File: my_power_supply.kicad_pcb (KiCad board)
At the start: 2 copper layers, 85 x 37.5 mm, 11 parts, among them U2 TPS54560BDDA, U3 HUSB238, U4 TPS54560BDDA

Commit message: V1 progress
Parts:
- added C1: 1u, Capacitor_SMD:C_1206_3216Metric, F.Cu at (113.0, 139.5)
- added J1: USB_C_Receptacle_USB2.0_16P, Connector_USB:USB_C_Receptacle_GCT_USB4135-GF-A_6P_TopMnt_Horizontal, F.Cu at (103.5, 132.2)
- moved R4 87.3 mm to (125.0, 129.6)
- moved R3 87.3 mm to (125.0, 126.3)
- moved R5 87.3 mm to (125.0, 132.9)
- moved R2 87.3 mm to (125.0, 123.0)
- moved R6 87.3 mm to (125.0, 136.2)
- moved R7 87.3 mm to (125.0, 139.4)
- moved R1 69.9 mm to (113.5, 122.0)
- moved R8 69.1 mm to (113.5, 125.0)
- moved U3 34.3 mm to (113.5, 131.5), turned to 180 degrees
- moved U2 29.5 mm to (146.3, 127.2)
- moved U4 27.3 mm to (146.2, 137.2)

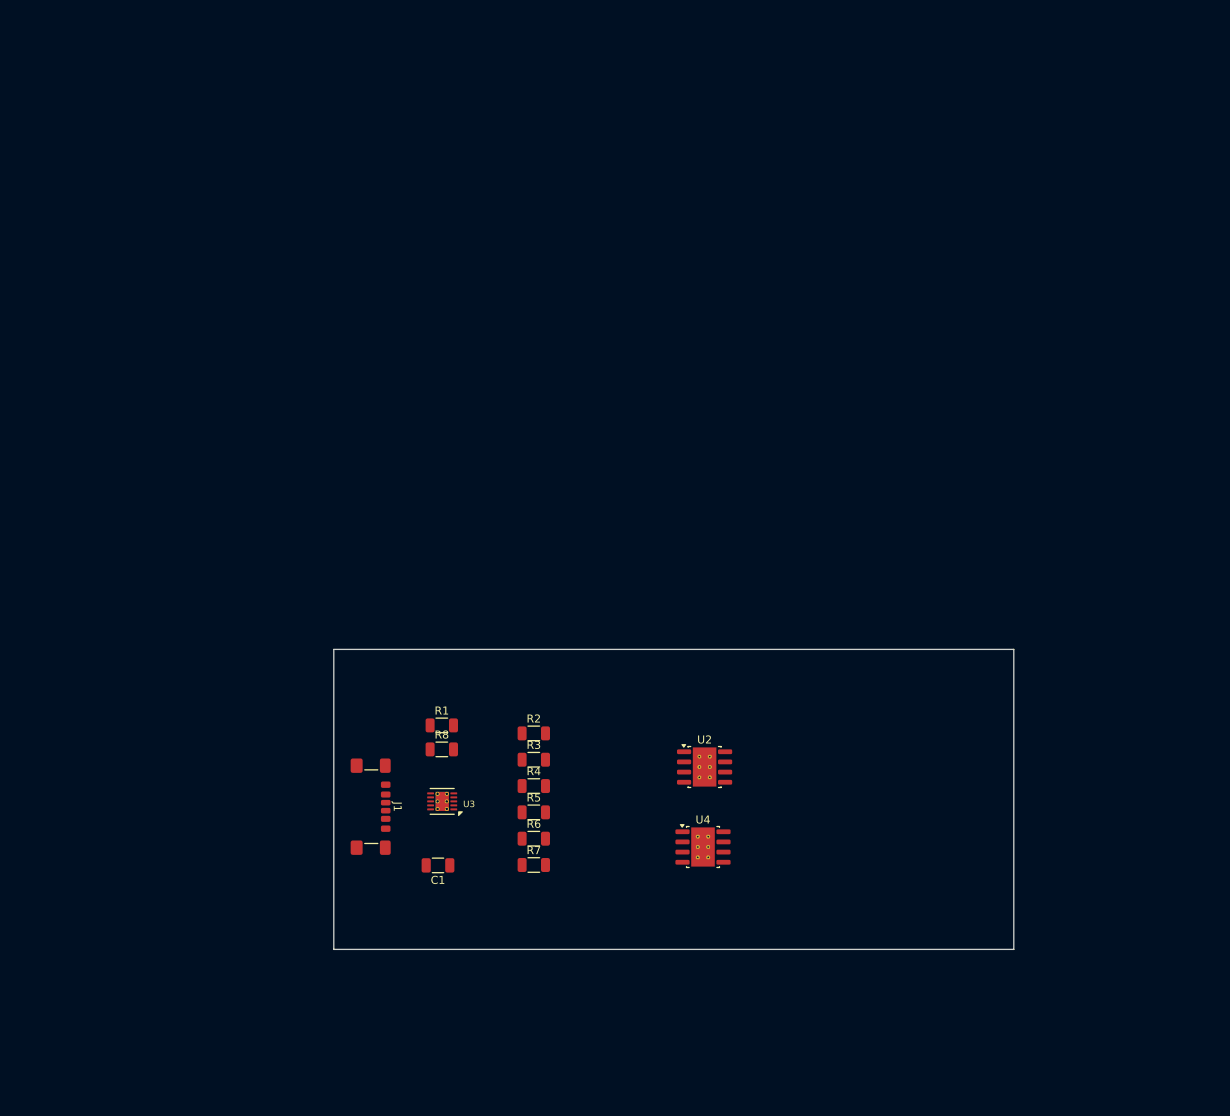
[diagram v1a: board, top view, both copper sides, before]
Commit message: Add footprints for some modules, everything has some kind of footprint to start. Beginning of layout
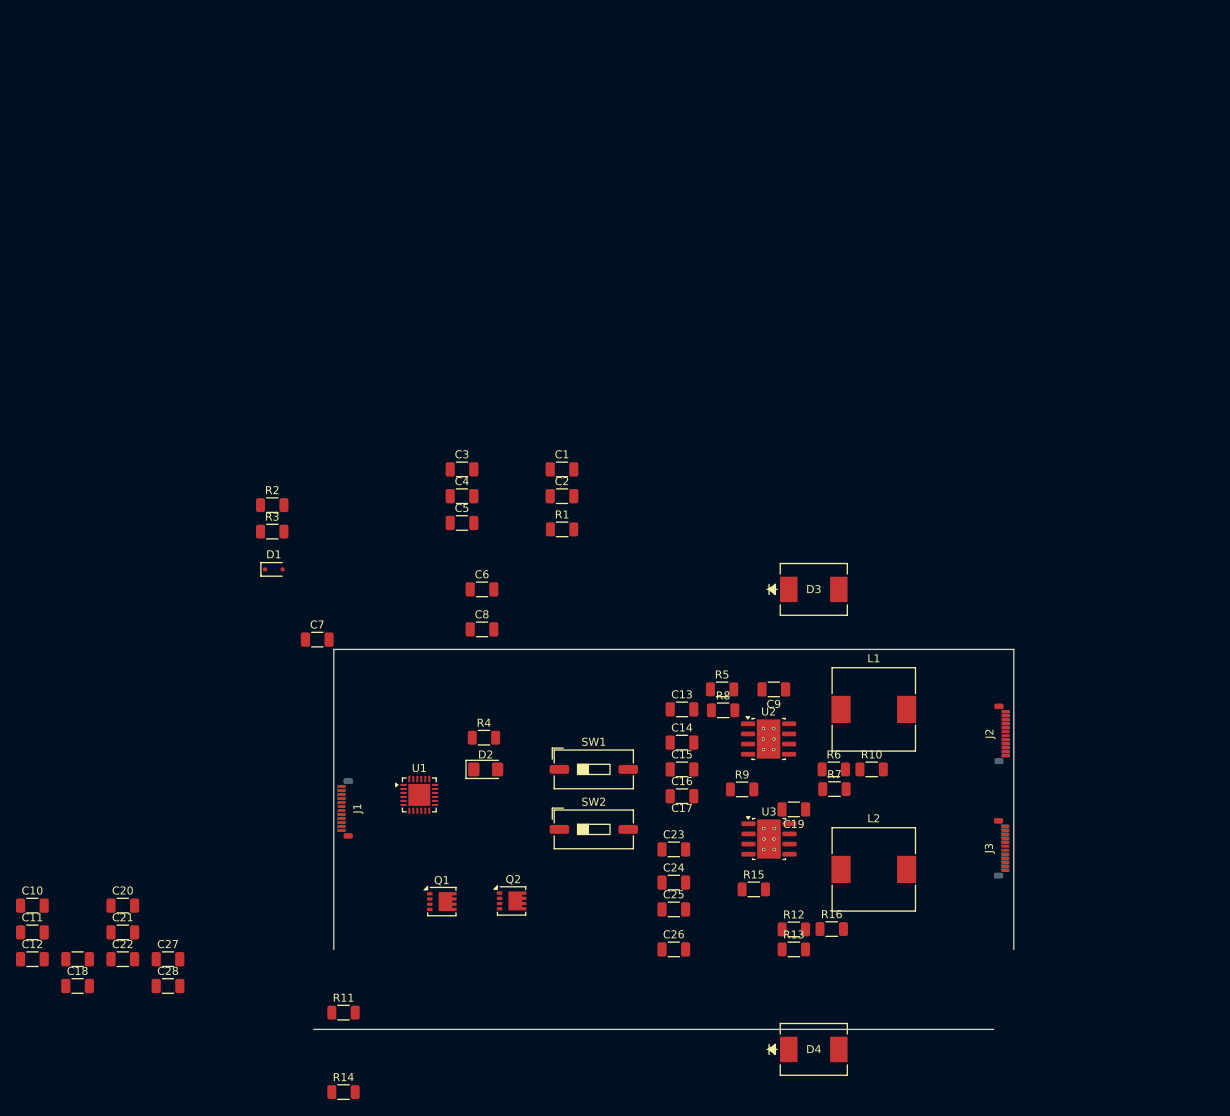
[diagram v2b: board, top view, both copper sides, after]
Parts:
- removed U4: TPS54560BDDA, Package_SO:Texas_R-PDSO-G8_EP2.95x4.9mm_Mask2.4x3.1mm_ThermalVias
- added C10: 47u, Capacitor_SMD:C_1206_3216Metric, F.Cu at (62.3, 144.5)
- added C11: 47u, Capacitor_SMD:C_1206_3216Metric, F.Cu at (62.3, 147.9)
- added C12: 47u, Capacitor_SMD:C_1206_3216Metric, F.Cu at (62.3, 151.2)
- added C13: 2.2u, Capacitor_SMD:C_1206_3216Metric, F.Cu at (143.5, 120.0)
- added C14: 2.2u, Capacitor_SMD:C_1206_3216Metric, F.Cu at (143.5, 124.2)
- added C15: 2.2u, Capacitor_SMD:C_1206_3216Metric, F.Cu at (143.5, 127.5)
- added C16: 2.2u, Capacitor_SMD:C_1206_3216Metric, F.Cu at (143.5, 130.8)
- added C17: 47p, Capacitor_SMD:C_1206_3216Metric, F.Cu at (68.0, 151.2)
- added C18: 4700p, Capacitor_SMD:C_1206_3216Metric, F.Cu at (68.0, 154.6)
- added C19: 0.1u, Capacitor_SMD:C_1206_3216Metric, F.Cu at (157.5, 132.5)
- added C2: 1u, Capacitor_SMD:C_1206_3216Metric, F.Cu at (128.5, 93.3)
- added C20: 47u, Capacitor_SMD:C_1206_3216Metric, F.Cu at (73.6, 144.5)
- added C21: 47u, Capacitor_SMD:C_1206_3216Metric, F.Cu at (73.6, 147.9)
- added C22: 47u, Capacitor_SMD:C_1206_3216Metric, F.Cu at (73.6, 151.2)
- added C23: 2.2u, Capacitor_SMD:C_1206_3216Metric, F.Cu at (142.5, 137.5)
- added C24: 2.2u, Capacitor_SMD:C_1206_3216Metric, F.Cu at (142.5, 141.7)
- added C25: 2.2u, Capacitor_SMD:C_1206_3216Metric, F.Cu at (142.5, 145.0)
- added C26: 2.2u, Capacitor_SMD:C_1206_3216Metric, F.Cu at (142.5, 150.0)
- added C27: 47p, Capacitor_SMD:C_1206_3216Metric, F.Cu at (79.3, 151.2)
- added C28: 4700p, Capacitor_SMD:C_1206_3216Metric, F.Cu at (79.3, 154.6)
- added C3: 1u, Capacitor_SMD:C_1206_3216Metric, F.Cu at (116.0, 90.0)
- added C4: 0.1u, Capacitor_SMD:C_1206_3216Metric, F.Cu at (116.0, 93.3)
- added C5: 0.1u, Capacitor_SMD:C_1206_3216Metric, F.Cu at (116.0, 96.7)
- added C6: 390p, Capacitor_SMD:C_1206_3216Metric, F.Cu at (118.5, 105.0)
- added C7: 1u, Capacitor_SMD:C_1206_3216Metric, F.Cu at (97.9, 111.3)
- added C8: 390p, Capacitor_SMD:C_1206_3216Metric, F.Cu at (118.5, 110.0)
- added C9: 0.1u, Capacitor_SMD:C_1206_3216Metric, F.Cu at (155.0, 117.5)
- added D1: D_Schottky, Diode_SMD:D_SOD-323F, F.Cu at (92.5, 102.5)
- added D2: LED_Small, LED_SMD:LED_1206_3216Metric_Pad1.42x1.75mm_HandSolder, F.Cu at (119.0, 127.5)
- added D3: D_Schottky, imported:SMC_DIO, F.Cu at (160.0, 105.0)
- added D4: D_Schottky, imported:SMC_DIO, F.Cu at (160.0, 162.5)
- added J2: USB_C_Receptacle_PowerOnly_6P, Connector_USB:USB_C_Plug_Molex_105444, F.Cu at (184.0, 123.0)
- added J3: USB_C_Receptacle_PowerOnly_6P, Connector_USB:USB_C_Plug_Molex_105444, F.Cu at (184.0, 137.4)
- added L1: 7.2u, imported:L_Wurth_WE-PDF-1045, F.Cu at (167.5, 120.0)
- added L2: 7.2u, imported:L_Wurth_WE-PDF-1045, F.Cu at (167.5, 140.0)
- added Q1: DMP3013SFV, Package_SON:Diodes_PowerDI3333-8, F.Cu at (113.5, 144.0)
- added Q2: DMP3013SFV, Package_SON:Diodes_PowerDI3333-8, F.Cu at (122.2, 143.9)
- added R10: 10.2k, Resistor_SMD:R_1206_3216Metric, F.Cu at (167.2, 127.5)
- added R11: 442k, Resistor_SMD:R_1206_3216Metric, F.Cu at (101.2, 157.9)
- added R12: 53.6k, Resistor_SMD:R_1206_3216Metric, F.Cu at (157.5, 147.5)
- added R13: 16.9k, Resistor_SMD:R_1206_3216Metric, F.Cu at (157.5, 150.0)
- added R14: 90.9k, Resistor_SMD:R_1206_3216Metric, F.Cu at (101.2, 167.8)
- added R15: 243k, Resistor_SMD:R_1206_3216Metric, F.Cu at (152.5, 142.5)
- added R16: 10.2k, Resistor_SMD:R_1206_3216Metric, F.Cu at (162.2, 147.5)
- added R9: 243k, Resistor_SMD:R_1206_3216Metric, F.Cu at (151.0, 130.0)
- added SW1: SW_SPST, Button_Switch_SMD:SW_DIP_SPSTx01_Slide_9.78x4.72mm_W8.61mm_P2.54mm, F.Cu at (132.5, 127.5)
- added SW2: SW_SPST, Button_Switch_SMD:SW_DIP_SPSTx01_Slide_9.78x4.72mm_W8.61mm_P2.54mm, F.Cu at (132.5, 135.0)
- added U1: CYPD3177-24LQ, Package_DFN_QFN:QFN-24-1EP_4x4mm_P0.5mm_EP2.75x2.75mm, F.Cu at (110.7, 130.7)
- C1: value 1u -> 3.3u
- J1: footprint Connector_USB:USB_C_Receptacle_GCT_USB4135-GF-A_6P_TopMnt_Horizontal -> Connector_USB:USB_C_Plug_Molex_105444
- R1: value 10 -> 10k
- R2: value 5.1k -> 47k
- R3: value 49.9k -> 1k
- R4: value 14k -> 2.4k
- R5: value 6k -> 442k
- R6: value 10k -> 53.6k
- R7: value 14k -> 16.9k
- R8: value 18k -> 90.9k
- U3: value HUSB238 -> TPS54560BDDA; footprint HUSB238:DFN-10-1EP_3x3mm_P0.5mm_EP1.65x2.38mm_ThermalVias -> Package_SO:Texas_R-PDSO-G8_EP2.95x4.9mm_Mask2.4x3.1mm_ThermalVias
- moved C1 51.9 mm to (128.5, 90.0), turned to 0 degrees
- moved R2 43.4 mm to (92.3, 94.5)
- moved R3 43.4 mm to (92.3, 97.8)
- moved U3 41.1 mm to (154.4, 136.2), turned to 0 degrees
- moved R7 38.8 mm to (162.6, 130.0)
- moved R6 38.5 mm to (162.5, 127.5)
- moved R8 35.5 mm to (148.7, 120.1)
- moved R1 28.7 mm to (128.5, 97.5)
- moved R5 28.1 mm to (148.5, 117.5)
- moved U2 8.73 mm to (154.3, 123.7)
- moved R4 8.68 mm to (118.8, 123.5)
- moved J1 2.55 mm to (100.9, 132.4), turned to 90 degrees
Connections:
- C1 pad 1: Net-(U3-VIN) -> VBUSIN
- J1 pad A5: /CC1 -> CC1
- J1 pad A9: Net-(J1-VBUS-PadA4) -> VBUSIN
- J1 pad B5: /CC2 -> CC2
- J1 pad B9: Net-(J1-VBUS-PadA4) -> VBUSIN
- R1 pad 1: Net-(J1-VBUS-PadA4) -> Net-(D1-A)
- R1 pad 2: Net-(U3-VIN) -> VBUSIN
- R2 pad 1: Net-(U3-GATE) -> Net-(D1-A)
- R2 pad 2: Net-(Q1-Pad4) -> Net-(D1-K)
- R3 pad 1: Net-(J1-VBUS-PadA4) -> Net-(U1-VBUS_FET_EN)
- R3 pad 2: Net-(Q1-Pad4) -> Net-(D1-A)
- R4 pad 2: Net-(JP6-A) -> Net-(D2-A)
- R5 pad 1: Net-(JP2-A) -> VCC1
- R5 pad 2: Net-(JP1-A) -> Net-(U2-EN)
- R6 pad 1: Net-(JP3-A) -> VOUT1
- R6 pad 2: Net-(JP1-A) -> FB1
- R7 pad 1: Net-(JP4-A) -> Net-(U2-COMP)
- R7 pad 2: Net-(JP1-A) -> Net-(C18-Pad2)
- R8 pad 1: Net-(JP5-A) -> Net-(U2-EN)
- R8 pad 2: Net-(JP1-A) -> GND
- U3 pad 1: Net-(U3-VIN) -> Net-(U3-BOOT)
- U3 pad 2: /D+ -> VCC2
- U3 pad 3: /D- -> Net-(U3-EN)
- U3 pad 4: /CC1 -> Net-(U3-RT/CLK)
- U3 pad 5: /CC2 -> FB2
- U3 pad 6: unconnected-(U3-SDA-Pad6) -> Net-(U3-COMP)
- U3 pad 7: unconnected-(U3-SCL-Pad7) -> GND
- U3 pad 8: Net-(JP1-A) -> Net-(D4-K)
- U3 pad 9: Net-(JP6-A) -> GND
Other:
- board size 85 x 37.5 mm -> 87.5 x 47.5 mm

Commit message: More PCB layout
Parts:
- moved C12 116.6 mm to (174.2, 118.2), turned to 90 degrees
- moved C11 113.4 mm to (171.8, 118.3), turned to 90 degrees
- moved C10 110.3 mm to (169.4, 118.2), turned to 90 degrees
- moved C17 105.3 mm to (169.1, 121.7), turned to 180 degrees
- moved C18 104.9 mm to (170.0, 130.0)
- moved C22 101.4 mm to (175.0, 152.5), turned to 90 degrees
- moved C21 99.0 mm to (172.5, 152.5), turned to 90 degrees
- moved C20 96.7 mm to (170.0, 152.5), turned to 90 degrees
- moved C27 90.6 mm to (169.7, 156.5), turned to 180 degrees
- moved C28 90.3 mm to (169.0, 165.0), turned to 180 degrees
- moved C1 62.9 mm to (92.4, 141.5), turned to 90 degrees
- moved C3 60.1 mm to (85.0, 141.5), turned to -90 degrees
- moved C2 58.8 mm to (94.8, 141.5), turned to 90 degrees
- moved C4 58.7 mm to (82.5, 141.5), turned to -90 degrees
- moved C5 57.5 mm to (80.0, 141.5), turned to -90 degrees
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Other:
- board outline removed

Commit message: Even more PCB layout
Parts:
- added R17: DNP, Resistor_SMD:R_1206_3216Metric, F.Cu at (93.0, 122.0)
- J1: footprint Connector_USB:USB_C_Plug_Molex_105444 -> Connector_USB:USB_C_Plug_JAE_DX07P024AJ1
- moved Q1 19.6 mm to (81.5, 139.3), turned to 180 degrees
- moved R3 17.0 mm to (90.0, 134.0)
- moved D1 16.8 mm to (85.9, 143.5)
- moved R2 13.2 mm to (94.5, 133.0)
- moved Q2 9.07 mm to (96.0, 138.4)
- moved C1 6.00 mm to (90.0, 147.0)
- moved R1 6.00 mm to (95.1, 147.0)
- moved C2 6.00 mm to (92.4, 147.0)
- moved C3 5.70 mm to (90.5, 140.0)
- moved C4 5.70 mm to (88.0, 140.0)
- moved C5 5.70 mm to (85.5, 140.0)
- moved C7 5.00 mm to (89.5, 136.5), turned to 180 degrees
- moved C8 2.50 mm to (81.0, 128.0)
- moved J1 1.98 mm to (75.5, 133.5), turned to -90 degrees
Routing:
- net Net-(D1-A): track 0.00 -> 17.1 mm
- net Net-(D1-K): track 0.00 -> 14.8 mm
- net CC1: track 0.00 -> 8.46 mm
- net 3V3: track 0.00 -> 7.89 mm
- net GND: track 0.00 -> 7.06 mm
- net Net-(U1-VCCD): track 0.00 -> 2.62 mm
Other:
- board outline added: 5 x 8.2 mm

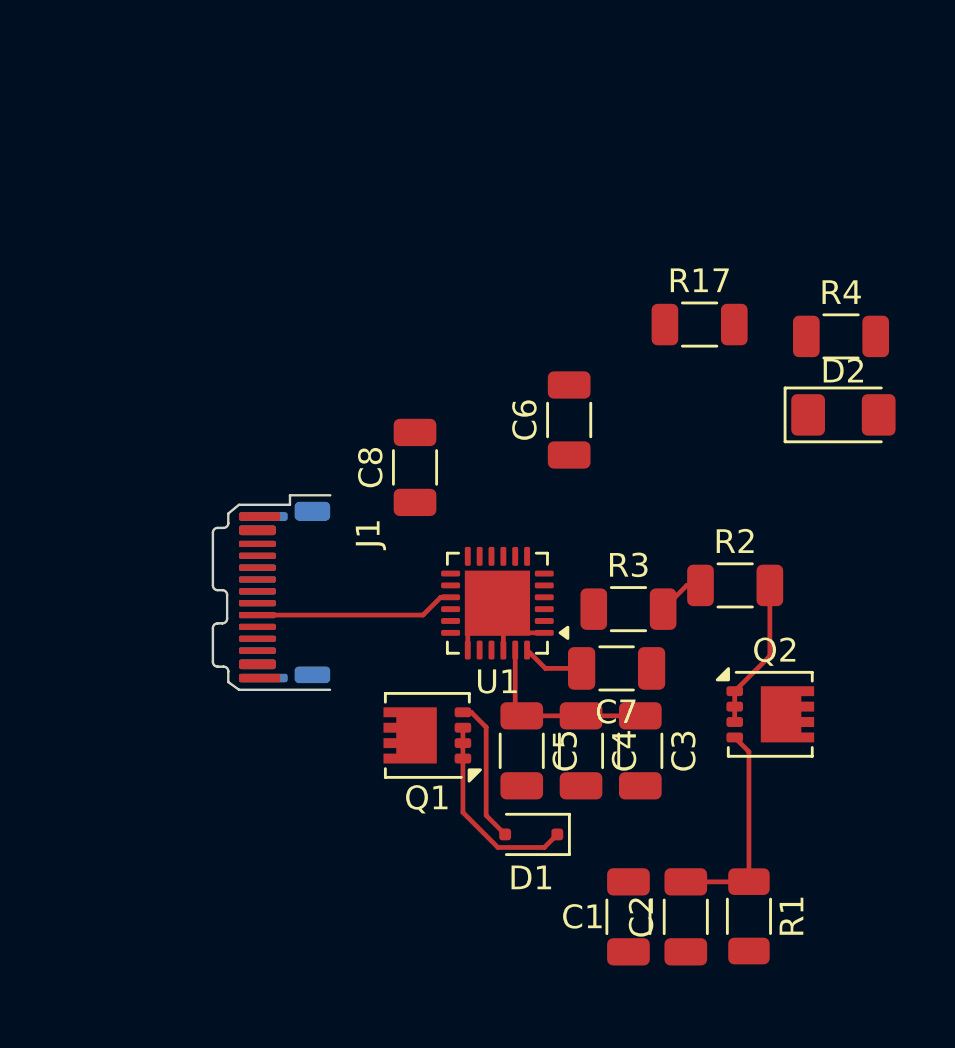
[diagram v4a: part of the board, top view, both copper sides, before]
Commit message: Voltage/Current setting resistors use DNF and 0
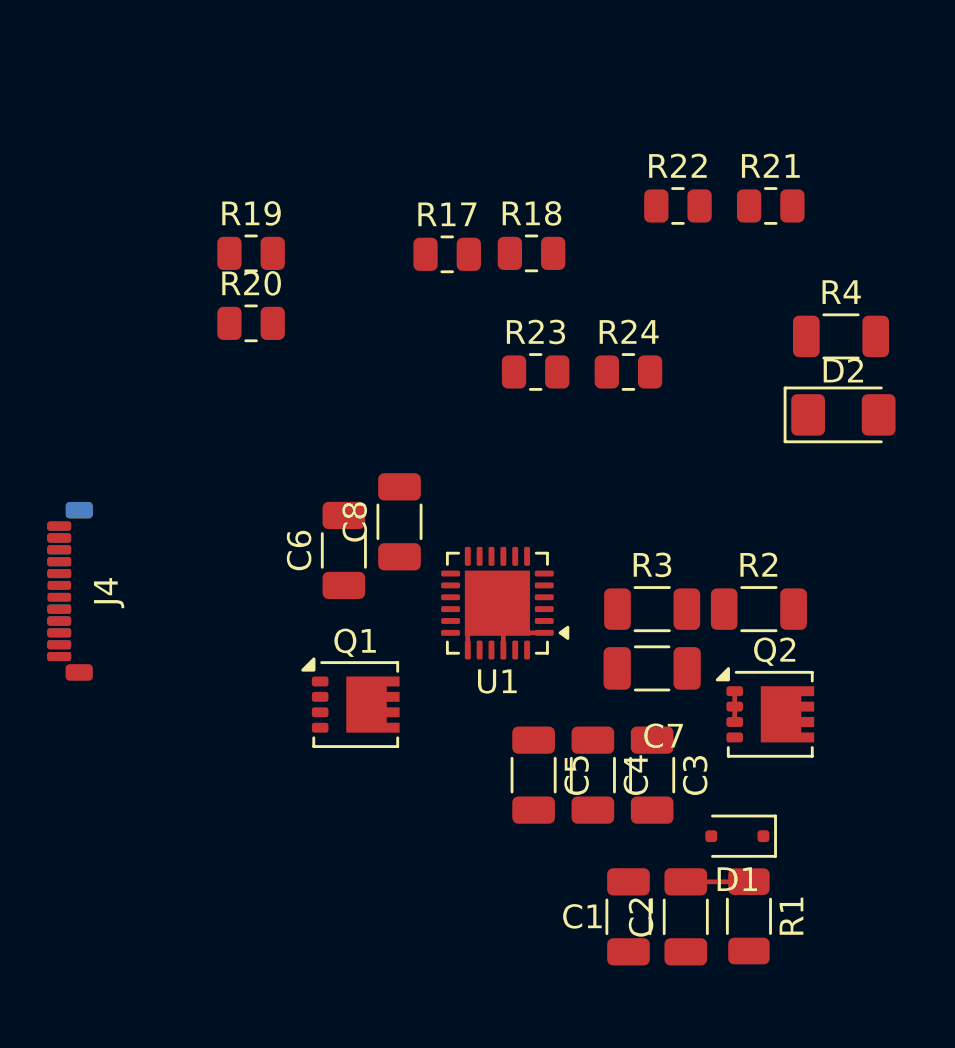
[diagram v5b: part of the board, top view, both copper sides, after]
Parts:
- removed J1: USB_C_Receptacle_USB2.0_16P, Connector_USB:USB_C_Plug_JAE_DX07P024AJ1
- added J4: USB_C_Receptacle_PowerOnly_6P, Connector_USB:USB_C_Plug_Molex_105444, F.Cu at (66.0, 133.2)
- added R18: 0, Resistor_SMD:R_0805_2012Metric, F.Cu at (85.9, 119.0)
- added R19: 0, Resistor_SMD:R_0805_2012Metric, F.Cu at (74.1, 119.0)
- added R20: DNP, Resistor_SMD:R_0805_2012Metric, F.Cu at (74.1, 122.0)
- added R21: DNP, Resistor_SMD:R_0805_2012Metric, F.Cu at (96.0, 117.0)
- added R22: 0, Resistor_SMD:R_0805_2012Metric, F.Cu at (92.1, 117.0)
- added R23: 0, Resistor_SMD:R_0805_2012Metric, F.Cu at (86.1, 124.0)
- added R24: DNP, Resistor_SMD:R_0805_2012Metric, F.Cu at (90.0, 124.0)
- D1: value D_Schottky -> NZH10C
- D3, D4: value D_Schottky -> B560C
- R17: footprint Resistor_SMD:R_1206_3216Metric -> Resistor_SMD:R_0805_2012Metric
- moved R17 11.0 mm to (82.4, 119.0)
- moved C6 11.0 mm to (78.0, 131.5)
- moved D1 8.69 mm to (94.6, 143.6)
- moved Q1 3.29 mm to (78.5, 138.0), turned to 0 degrees
- moved C8 2.38 mm to (80.3, 130.3)
- moved C7 1.50 mm to (91.0, 136.5)
- moved R2 1.41 mm to (95.5, 134.0)
- moved C3 1.14 mm to (91.0, 141.0)
- moved C4 1.14 mm to (88.5, 141.0)
- moved C5 1.14 mm to (86.0, 141.0)
- moved R3 1.00 mm to (91.0, 134.0)
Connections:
- R17 pad 2: 3V3 -> Net-(U1-VBUS_MAX)
- U1 pad 1: GND -> Net-(U1-VBUS_MIN)
- U1 pad 2: 3V3 -> Net-(U1-VBUS_MAX)
- U1 pad 5: 3V3 -> Net-(U1-ISNK_COARSE)
- U1 pad 6: GND -> Net-(U1-ISNK_FINE)
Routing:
- net Net-(D1-A): track 17.1 -> 2.67 mm
- net Net-(D1-K): track 14.8 -> 1.30 mm
- net CC1: track 8.46 -> 0.00 mm
- net 3V3: track 7.89 -> 0.00 mm
- net Net-(U1-VCCD): track 2.62 -> 0.00 mm
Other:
- board outline removed
